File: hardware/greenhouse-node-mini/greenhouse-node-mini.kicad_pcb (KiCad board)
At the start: 4 copper layers, 70 x 50 mm, 40 parts, among them J1 Molex_KK_396_1x2, J2 JST_XH_2.54mm_1x2, J4 Molex_KK_396_1x2, J5 JST_XH_2.54mm_1x4, J6 PinHeader_1x04_P2.54mm, J7 PinHeader_1x04_P2.54mm, Q1 A42, U1 ATtiny84A-P, U2 L7805, U3 PCF8574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

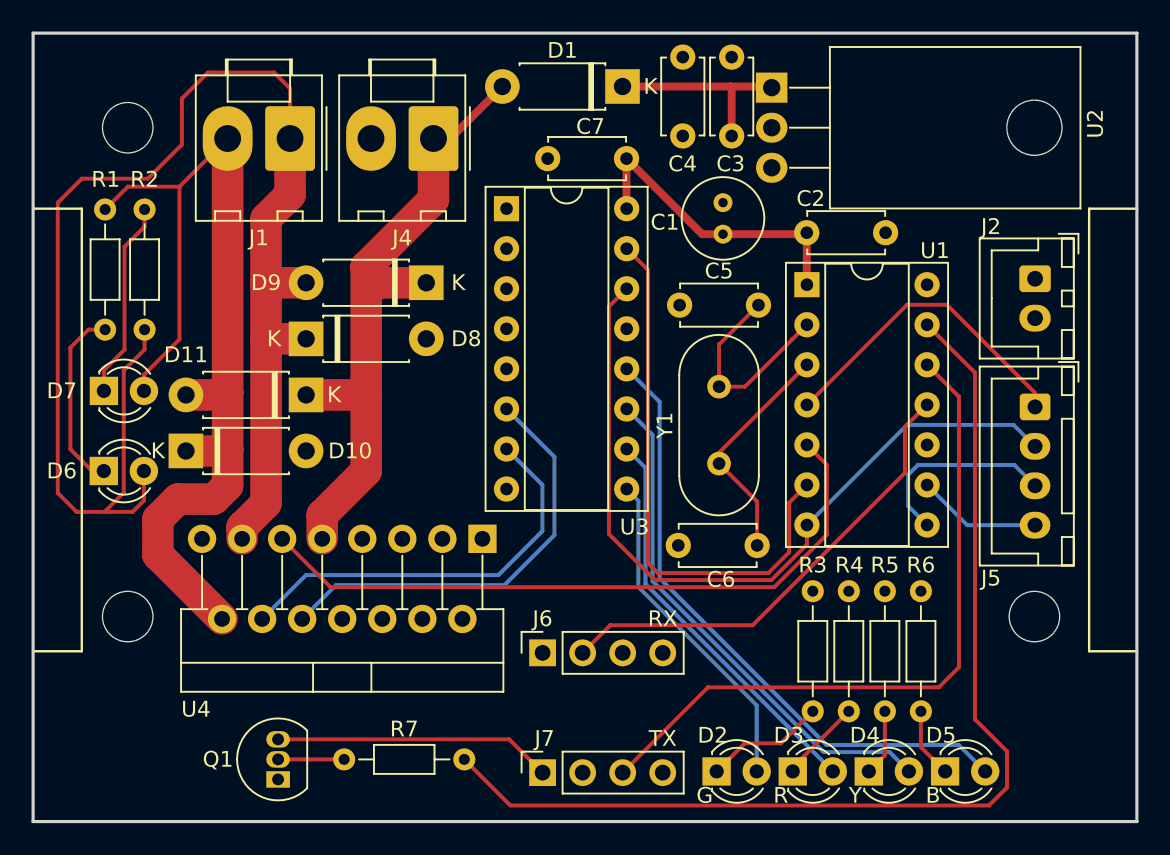
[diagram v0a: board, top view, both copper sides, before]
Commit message: Rearranged resistors
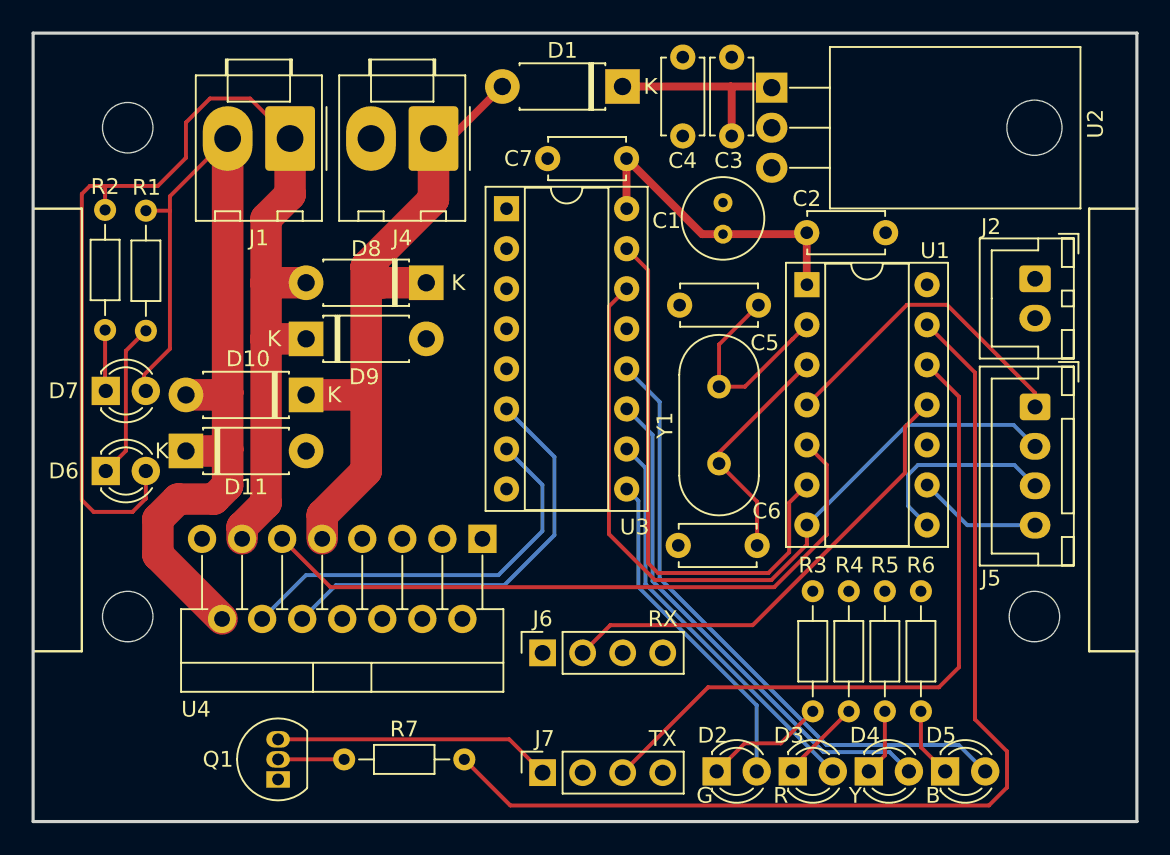
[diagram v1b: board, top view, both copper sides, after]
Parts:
- moved R2 8.00 mm to (70.6, 48.2), turned to -90 degrees
- moved R1 2.59 mm to (73.2, 48.3)
- moved D6 0.12 mm to (70.6, 64.8)
- moved D7 0.12 mm to (70.6, 59.7)
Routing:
- net /M_OUT1: track 94.3 -> 77.2 mm
- net Net-(D7-Pad1): track 12.6 -> 3.88 mm
- net /M_OUT2: track 64.2 -> 60.4 mm
- net Net-(D6-Pad1): track 11.1 -> 9.94 mm

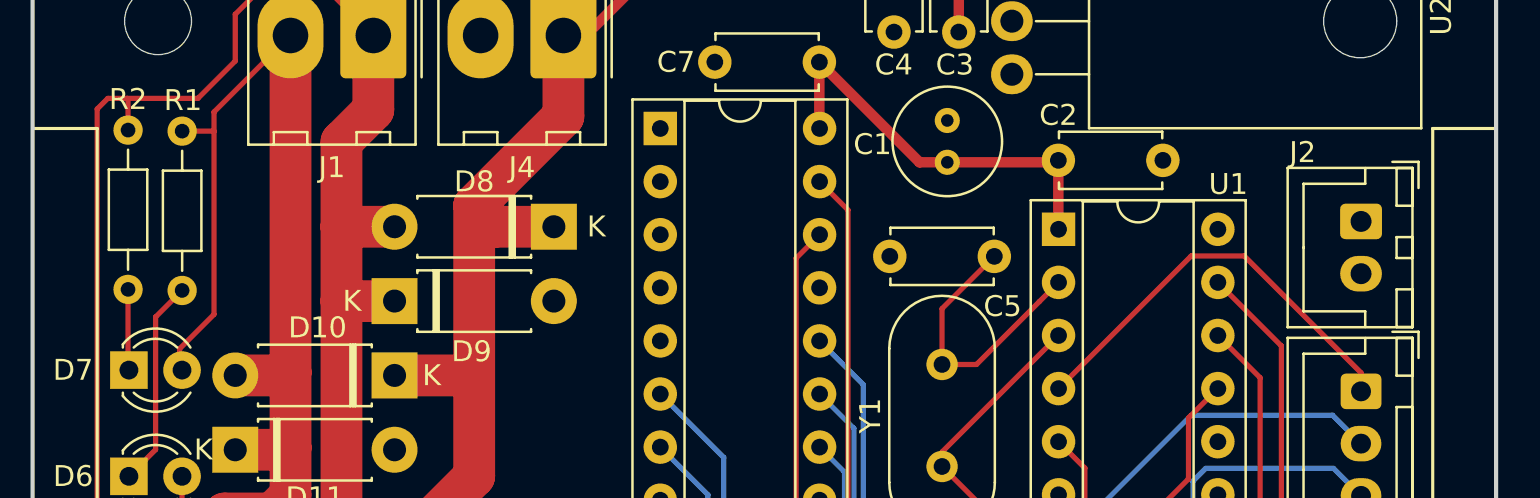
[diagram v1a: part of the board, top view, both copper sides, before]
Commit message: Swapped GND/PWR for IC programming connector
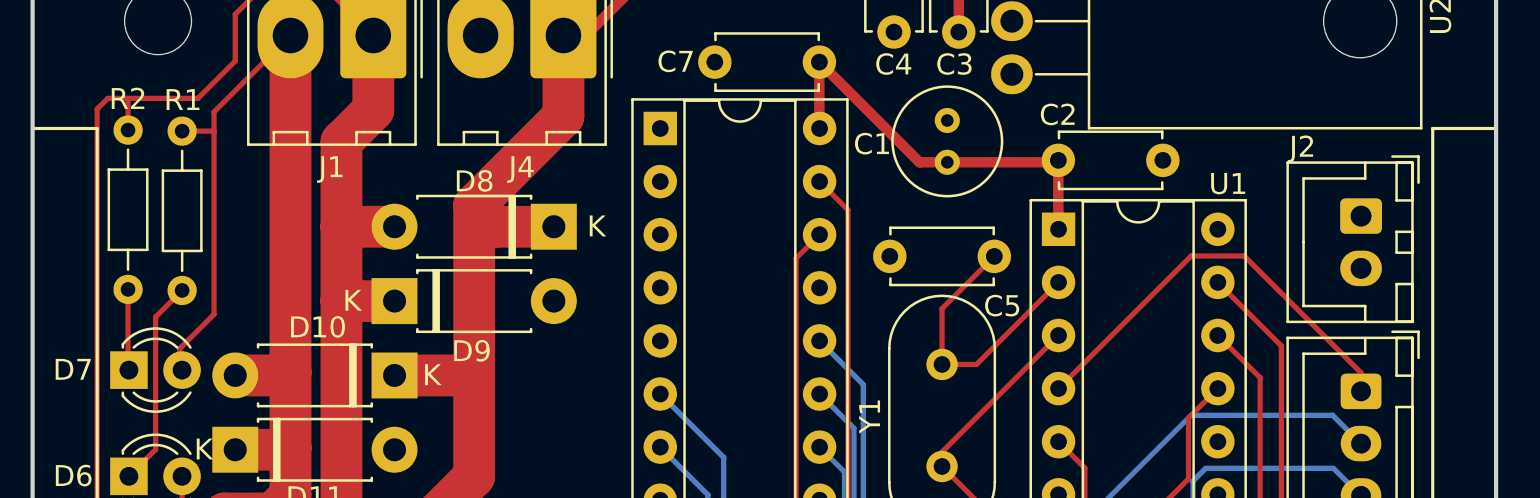
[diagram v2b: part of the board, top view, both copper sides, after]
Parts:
- moved J2 0.25 mm to (129.5, 52.3)
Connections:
- J2 pad 1: +5V -> GND
- J2 pad 2: GND -> +5V

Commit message: Tweak traces
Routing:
- net /PGM_C: track 7.91 -> 14.7 mm
- net /PGM_B: track 12.5 -> 7.88 mm
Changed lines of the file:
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@@
   (segment (start 121.417 61.849) (end 128.183 61.849) (width 0.25) (layer "B.Cu") (net 6))
   (segment (start 128.183 61.849) (end 129.54 63.206) (width 0.25) (layer "B.Cu") (net 6))
-  (segment (start 121.5 65) (end 121.5 67.002) (width 0.25) (layer "B.Cu") (net 7))
-  (segment (start 122.111 64.389) (end 121.5 65) (width 0.25) (layer "B.Cu") (net 7))
-  (segment (start 129.54 65.706) (end 128.223 64.389) (width 0.25) (layer "B.Cu") (net 7))
-  (segment (start 121.5 67.002) (end 122.692 68.194) (width 0.25) (layer "B.Cu") (net 7))
-  (segment (start 128.223 64.389) (end 122.111 64.389) (width 0.25) (layer "B.Cu") (net 7))
-  (segment (start 129.54 68.206) (end 125.244 68.206) (width 0.25) (layer "B.Cu") (net 8))
-  (segment (start 125.244 68.206) (end 122.692 65.654) (width 0.25) (layer "B.Cu") (net 8))
+  (segment (start 127.052 68.194) (end 122.692 68.194) (width 0.25) (layer "B.Cu") (net 7))
+  (segment (start 129.54 65.706) (end 127.052 68.194) (width 0.25) (layer "B.Cu") (net 7))
+  (segment (start 127.388 70.358) (end 121.666 70.358) (width 0.25) (layer "B.Cu") (net 8))
+  (segment (start 120.65 67.696) (end 122.692 65.654) (width 0.25) (layer "B.Cu") (net 8))
+  (segment (start 121.666 70.358) (end 120.65 69.342) (width 0.25) (layer "B.Cu") (net 8))
+  (segment (start 129.54 68.206) (end 127.388 70.358) (width 0.25) (layer "B.Cu") (net 8))
+  (segment (start 120.65 69.342) (end 120.65 67.696) (width 0.25) (layer "B.Cu") (net 8))
   (segment (start 124.714 60.056) (end 122.692 58.034) (width 0.25) (layer "F.Cu") (net 9))
   (segment (start 123.444 78.486) (end 124.714 77.216) (width 0.25) (layer "F.Cu") (net 9))
